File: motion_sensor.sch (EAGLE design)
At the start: 47 parts, among them J1 AVR_SPI_PRG_6PTH, J2 FTDI_DEVICERA_SMT, U1 LP2985A-33DBVTE4, U2 nRF8001, U3 ATMEGA328P_TQFP, Y1 16MHz, Y2 FC-255 32.7680K-A3, Y4 16MHz

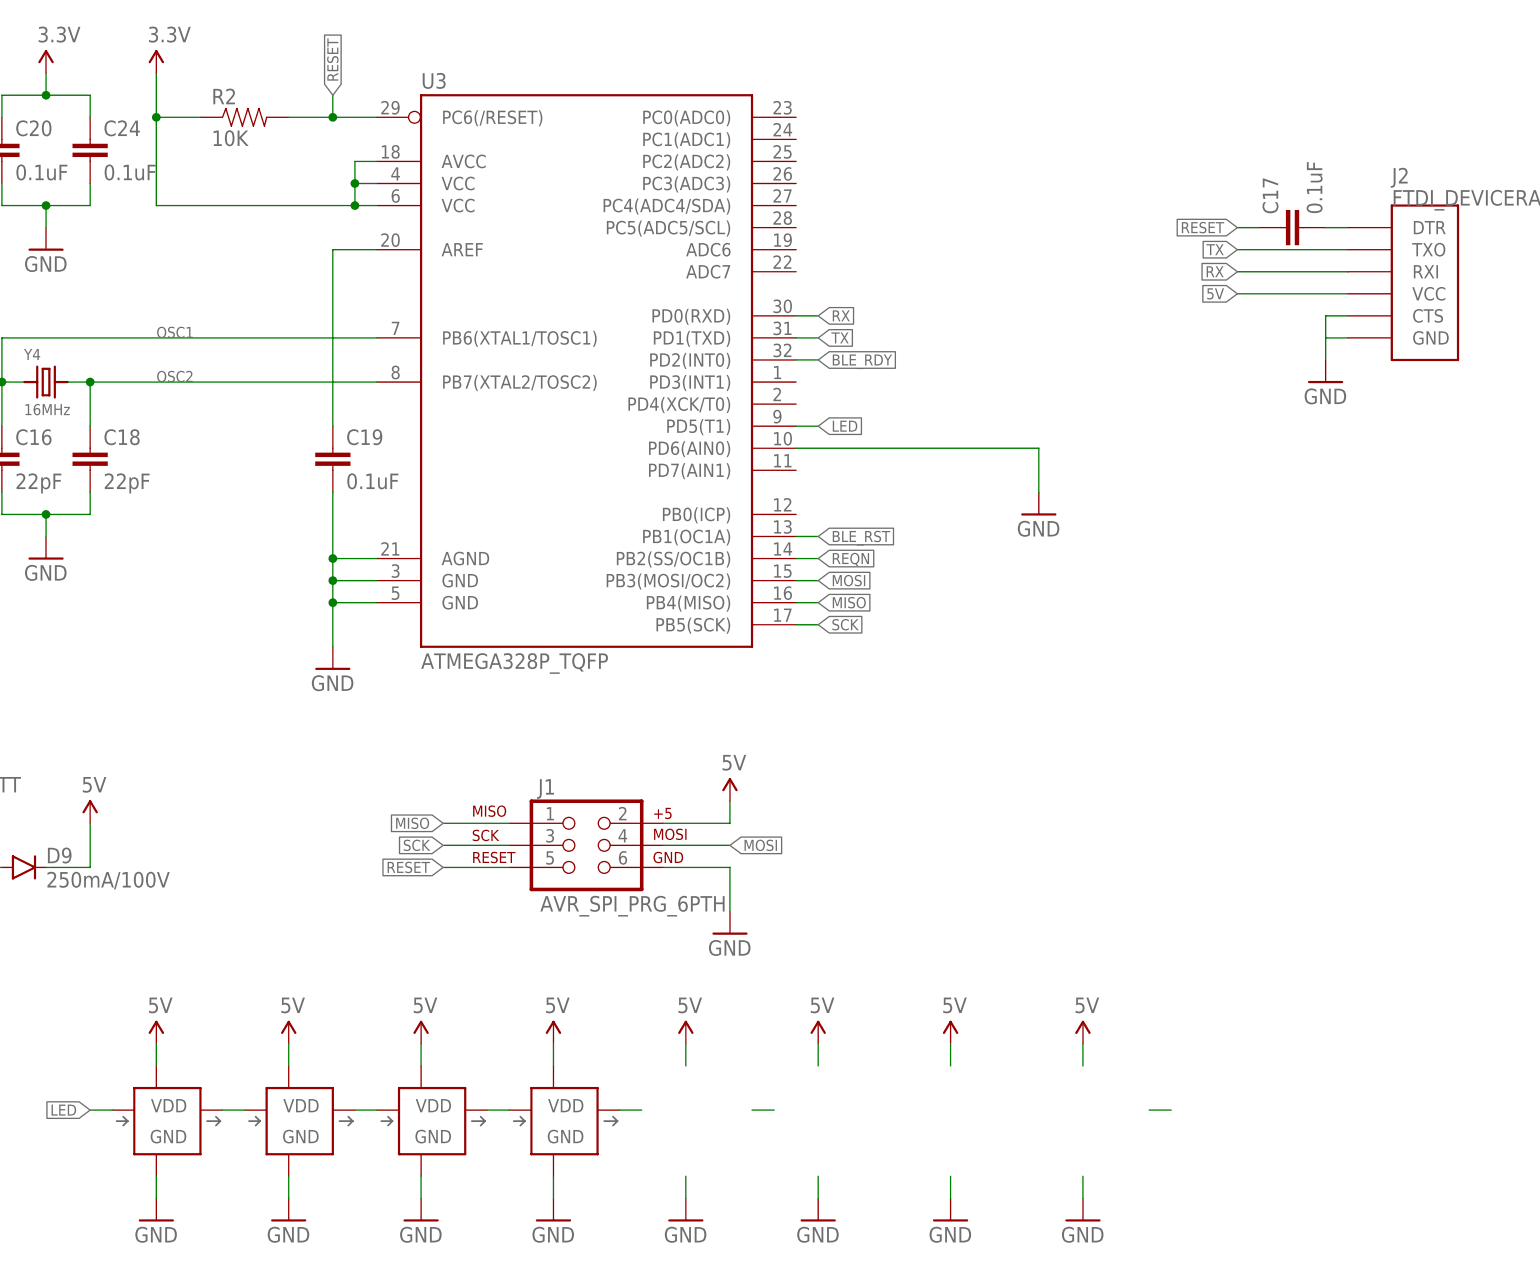
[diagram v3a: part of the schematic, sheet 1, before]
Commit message: Respin board to be 35mm square. Better antenna. Less things near the antenna.
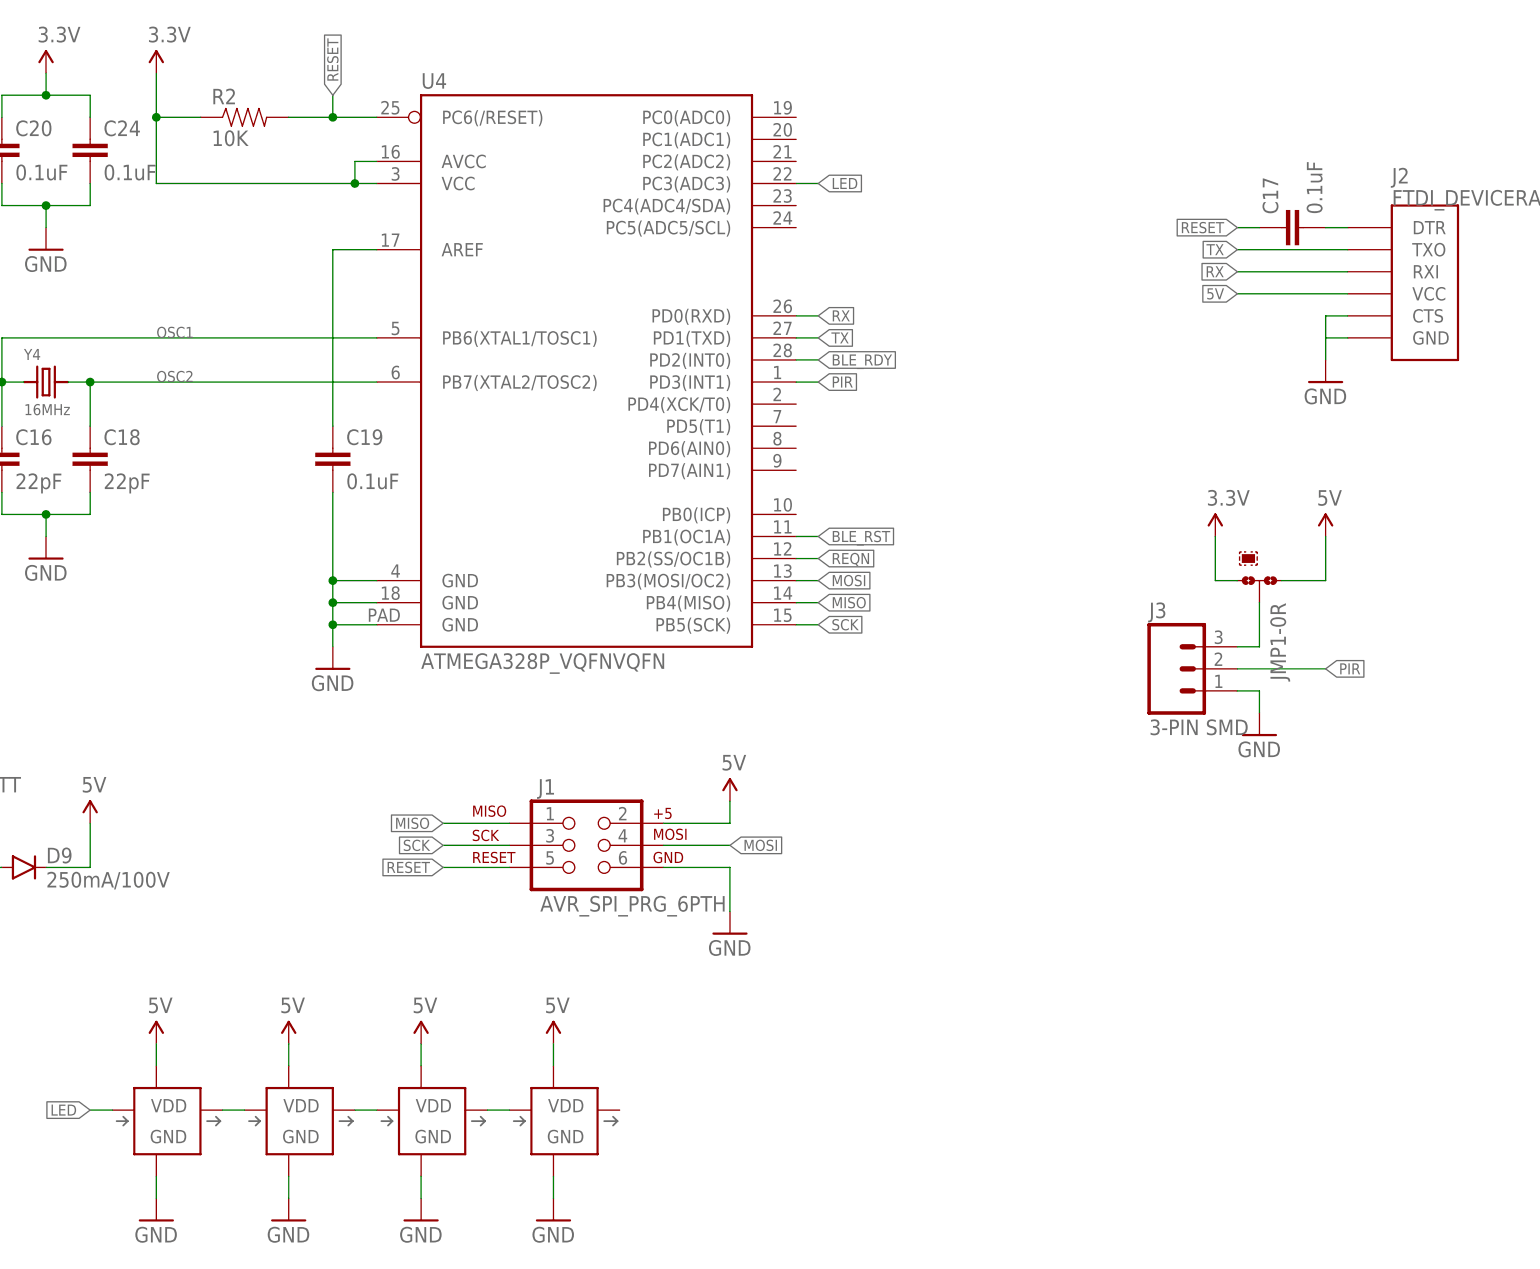
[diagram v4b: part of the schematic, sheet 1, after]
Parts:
- removed U$28: (no value), microbuilder:ANTENNA_PCBNRF8001_1.6MM
- removed U3: ATMEGA328P_TQFP, SparkFun-DigitalIC:ATMEGA328P_TQFP
- added E1: ANTENNATRACE, SparkFun-RF:ANTENNATRACE
- added J3: 3-PIN SMD, SparkFun-Connectors:M03JST-SMD
- added JMP1: 0R-JUMPC, jump-0r-smd:0R-JUMPC
- added U4: ATMEGA328P_VQFNVQFN, SparkFun-DigitalIC:ATMEGA328P_VQFNVQFN
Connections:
- net N$1 renamed DEC2
- net N$10 renamed XC2
- net N$11 renamed DCC
- net N$22 renamed XL2
- net N$23 renamed XL1
- net N$27 renamed BYPASS
- net N$3 renamed ???
- net N$8 renamed DEC1
- net N$9 renamed XC1
- removed net N$12: U$17.DO
- removed net N$24: C19.1, U3.AREF
- new net AREF: C19.1, U4.AREF
- new net PIR: J3.2, U4.PD3(INT1)
- new net PIR_VDD: J3.3, JMP1-0R.2
- net 3.3V: now also JMP1-0R.3, U4.AVCC, U4.VCC; no longer U3.AVCC, U3.VCC@4, U3.VCC@6
- net 5V: now also JMP1-0R.1
- net BLE_RDY: now also U4.PD2(INT0); no longer U3.PD2(INT0)
- net BLE_RST: now also U4.PB1(OC1A); no longer U3.PB1(OC1A)
- net GND: now also E1.GND, J3.1, U4.GND@1, U4.GND@2, U4.GND@PAD; no longer U3.AGND, U3.GND@3, U3.GND@5, U3.PD6(AIN0)
- net LED: now also U4.PC3(ADC3); no longer U3.PD5(T1)
- net MISO: now also U4.PB4(MISO); no longer U3.PB4(MISO)
- net MOSI: now also U4.PB3(MOSI/OC2); no longer U3.PB3(MOSI/OC2)
- net N$20: now also E1.SIGNAL; no longer U$28.P$1
- net OSC1: now also U4.PB6(XTAL1/TOSC1); no longer U3.PB6(XTAL1/TOSC1)
- net OSC2: now also U4.PB7(XTAL2/TOSC2); no longer U3.PB7(XTAL2/TOSC2)
- net REQN: now also U4.PB2(SS/OC1B); no longer U3.PB2(SS/OC1B)
- net RESET: now also U4.PC6(/RESET); no longer U3.PC6(/RESET)
- net RX: now also U4.PD0(RXD); no longer U3.PD0(RXD)
- net SCK: now also U4.PB5(SCK); no longer U3.PB5(SCK)
- net TX: now also U4.PD1(TXD); no longer U3.PD1(TXD)

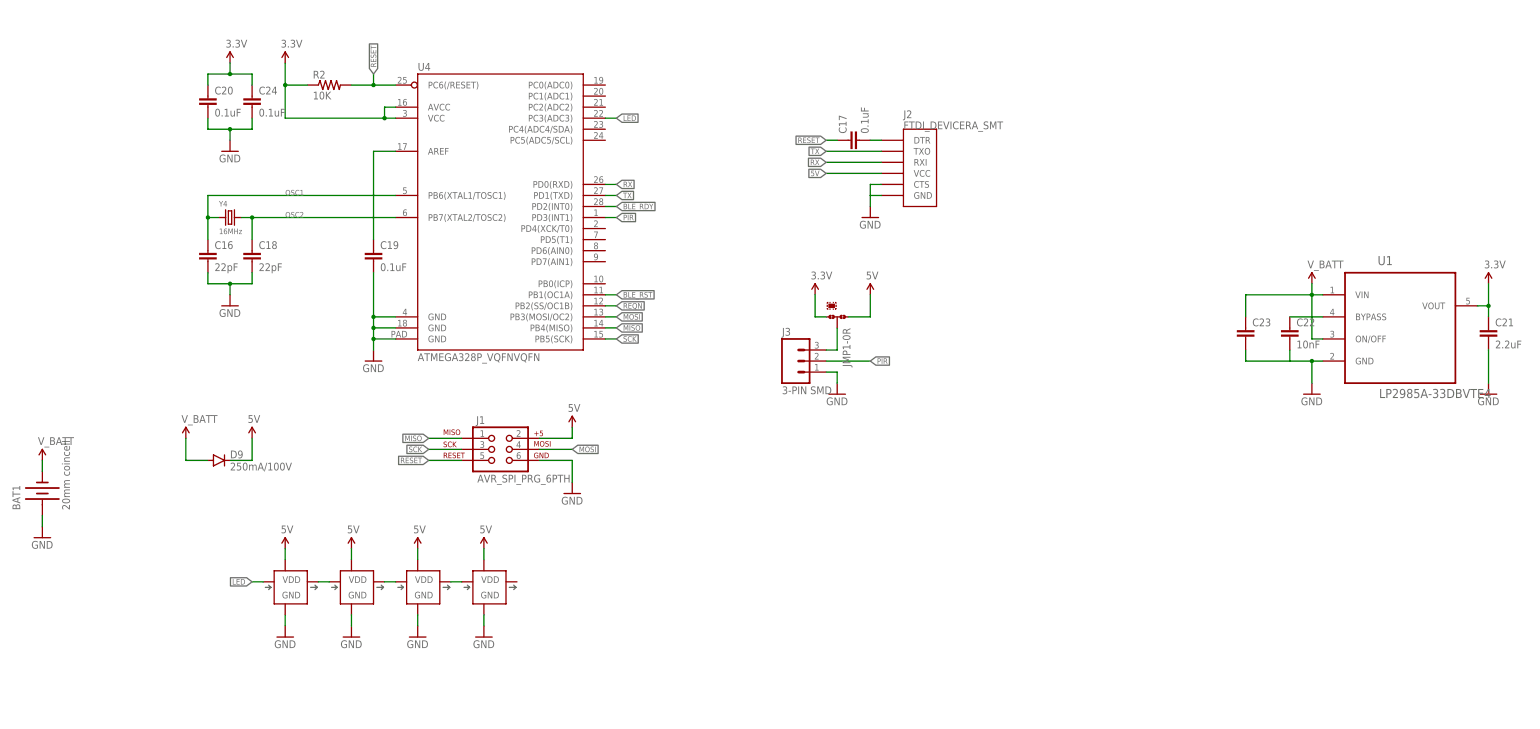
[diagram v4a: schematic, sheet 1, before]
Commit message: Add OSH logo. Add png versions of schematic and pcb.
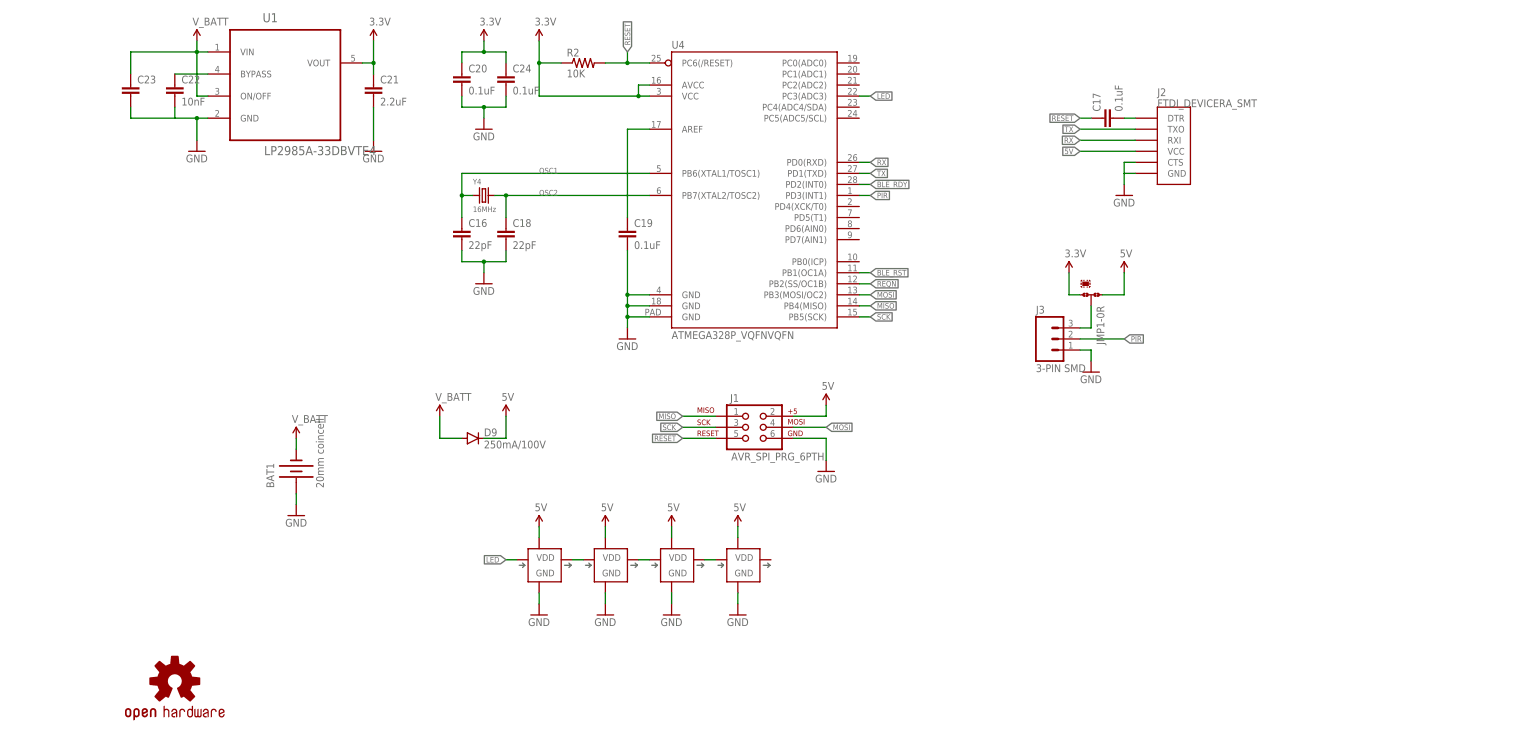
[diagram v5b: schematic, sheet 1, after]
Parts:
- added LOGO1: OSHW-LOGOS, SparkFun-Aesthetics:OSHW-LOGOS
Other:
- moved on the sheet: BAT1, C1, C10, C11, C12, C13, C14, C15, C16, C17, C18, C19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
